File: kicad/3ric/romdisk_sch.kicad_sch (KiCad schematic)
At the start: 54 parts

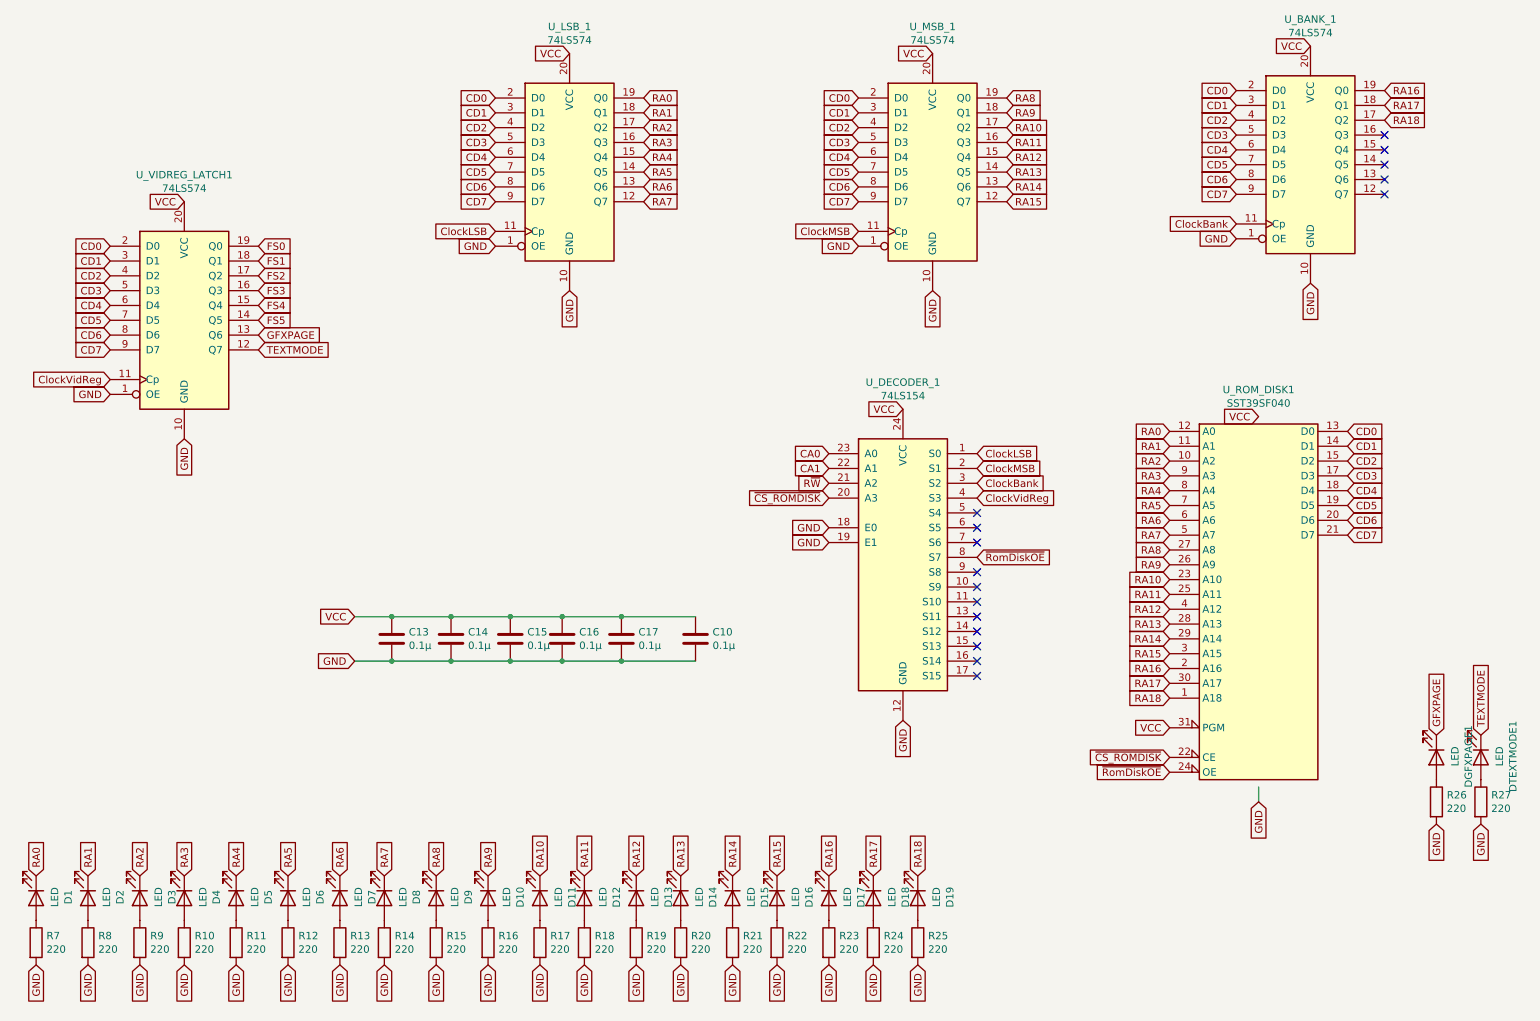
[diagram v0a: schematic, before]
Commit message: schematic updates - bring the schematics up to match breadboard changes current state has high res Apple II color emulation working
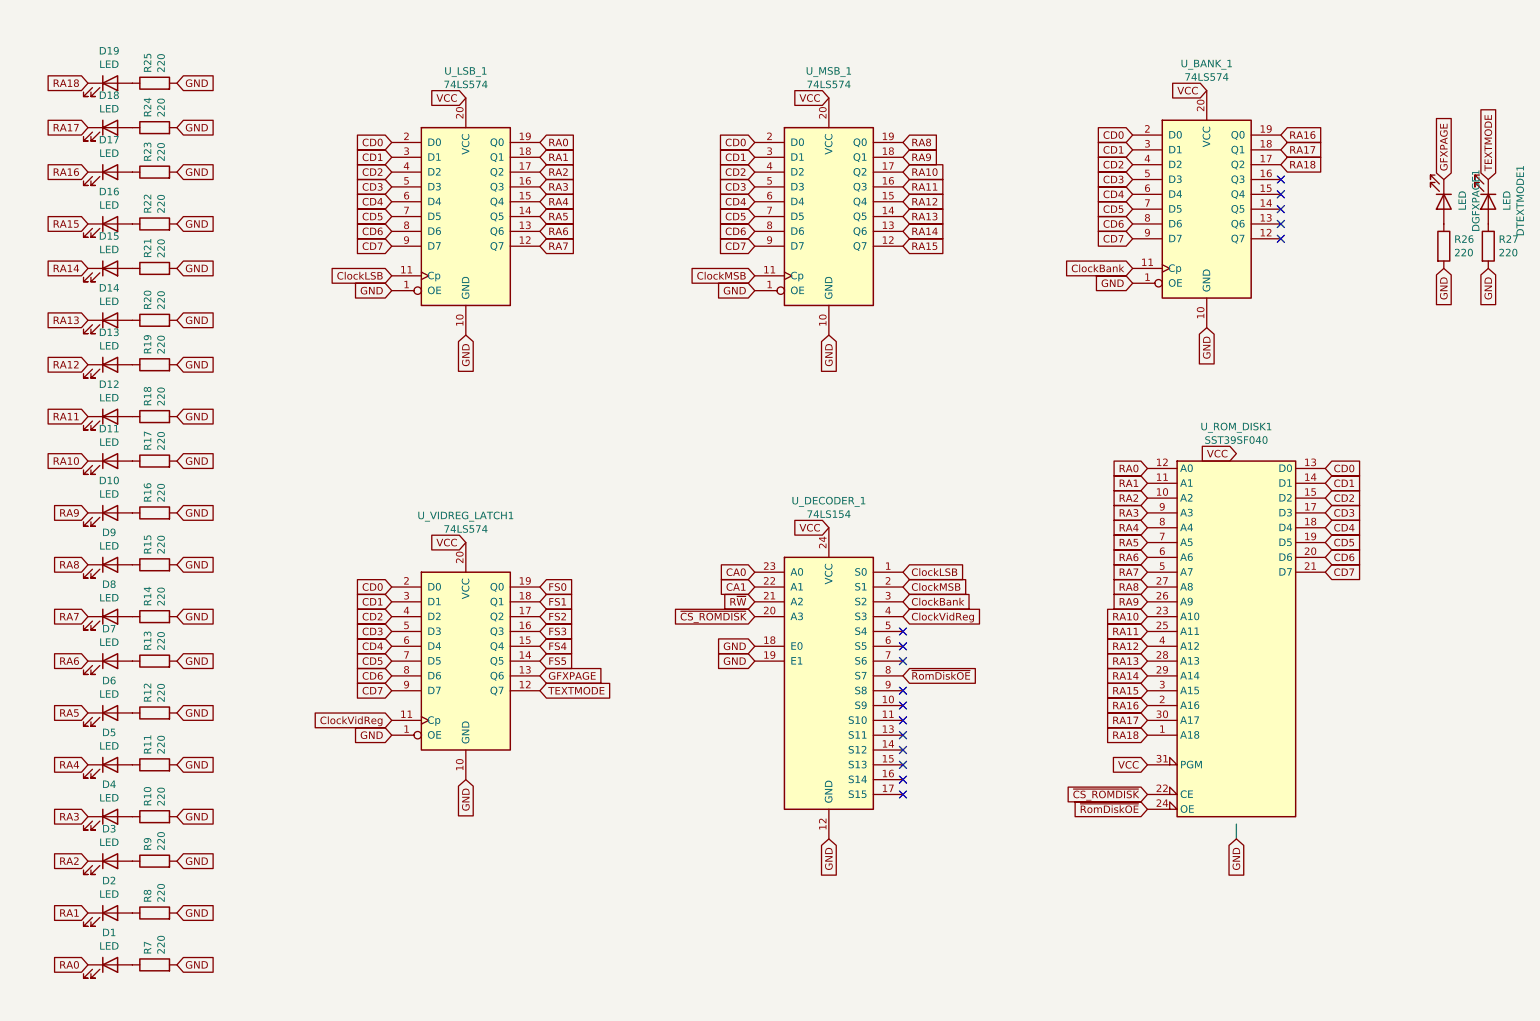
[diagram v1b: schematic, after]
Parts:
- removed C10, C13, C14, C15, C16, C17: 0.1µ, Capacitor_THT:C_Axial_L3.8mm_D2.6mm_P7.50mm_Horizontal, symbol Device:C
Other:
- moved on the sheet: D1, D10, D11, D12, D13, D14, D15, D16, D17, D18, D19, D2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

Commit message: updates to logisim project and schematics
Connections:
- net GFXPAGE: no longer U_VIDREG_LATCH1.13 (Q6)
- net TEXTMODE: no longer U_VIDREG_LATCH1.12 (Q7)
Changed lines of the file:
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@@
-    )
-  )
-  (global_label "TEXTMODE" (shape input) (at 107.95 130.81 0) (fields_autoplaced)
-    (effects (font (size 1.27 1.27)) (justify left))
-    (property "Intersheet References" "${INTERSHEET_REFS}" (id 0) (at 119.8579 130.7306 0)
-      (effects (font (size 1.27 1.27)) (justify left) hide)
     )
   )
@@
     )
   )
-  (global_label "GFXPAGE" (shape input) (at 107.95 128.27 0) (fields_autoplaced)
-    (effects (font (size 1.27 1.27)) (justify left))
-    (property "Intersheet References" "${INTERSHEET_REFS}" (id 0) (at 118.7088 128.1906 0)
-      (effects (font (size 1.27 1.27)) (justify left) hide)
-    )
-  )

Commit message: update schematics
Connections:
- net FS6: now reaches U_VIDREG_LATCH1.13 (Q6)
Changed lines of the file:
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@@
 (kicad_sch (version 20211123) (generator eeschema)
   (paper "A4")
-  (no_connect (at 170.18 130.81))
   (no_connect (at 170.18 148.59))
   (no_connect (at 170.18 140.97))
   (no_connect (at 170.18 133.35))
   (no_connect (at 170.18 135.89))
+  (no_connect (at 170.18 130.81))
   (no_connect (at 170.18 146.05))
   (no_connect (at 170.18 143.51))
@@
     )
   )
+  (global_label "~{RomDiskOE}" (shape input) (at 170.18 128.27 0) (fields_autoplaced)
+    (effects (font (size 1.27 1.27)) (justify left))
+    (property "Intersheet References" "${INTERSHEET_REFS}" (id 0) (at -8.89 11.43 0)
+      (effects (font (size 1.27 1.27)) hide)
+    )
+  )
   (global_label "GND" (shape input) (at 209.55 60.96 180) (fields_autoplaced)
     (effects (font (size 1.27 1.27)) (justify right))
@@
     )
   )
+  (global_label "FS6" (shape input) (at 107.95 128.27 0) (fields_autoplaced)
+    (effects (font (size 1.27 1.27)) (justify left))
+    (property "Intersheet References" "${INTERSHEET_REFS}" (id 0) (at 113.8707 128.1906 0)
+      (effects (font (size 1.27 1.27)) (justify left) hide)
+    )
+  )
   (global_label "RA8" (shape input) (at 30.48 109.22 180) (fields_autoplaced)
     (effects (font (size 1.27 1.27)) (justify right))
@@
     )
   )
-  (global_label "~{RomDiskOE}" (shape input) (at 170.18 128.27 0) (fields_autoplaced)
-    (effects (font (size 1.27 1.27)) (justify left))
-    (property "Intersheet References" "${INTERSHEET_REFS}" (id 0) (at -8.89 11.43 0)
-      (effects (font (size 1.27 1.27)) hide)
-    )
-  )

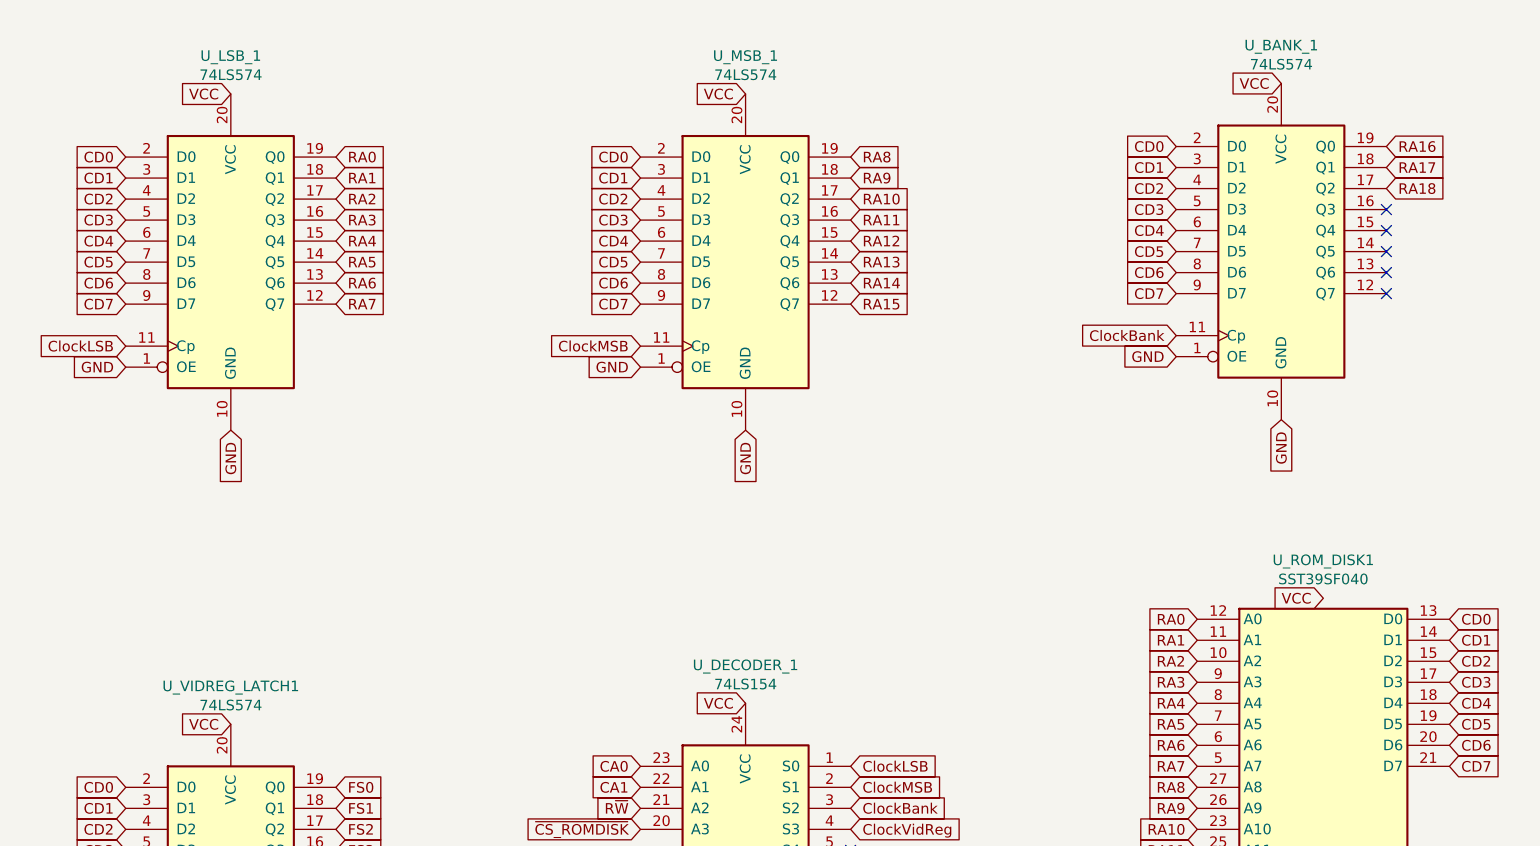
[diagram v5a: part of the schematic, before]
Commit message: update schematic based on breadboard
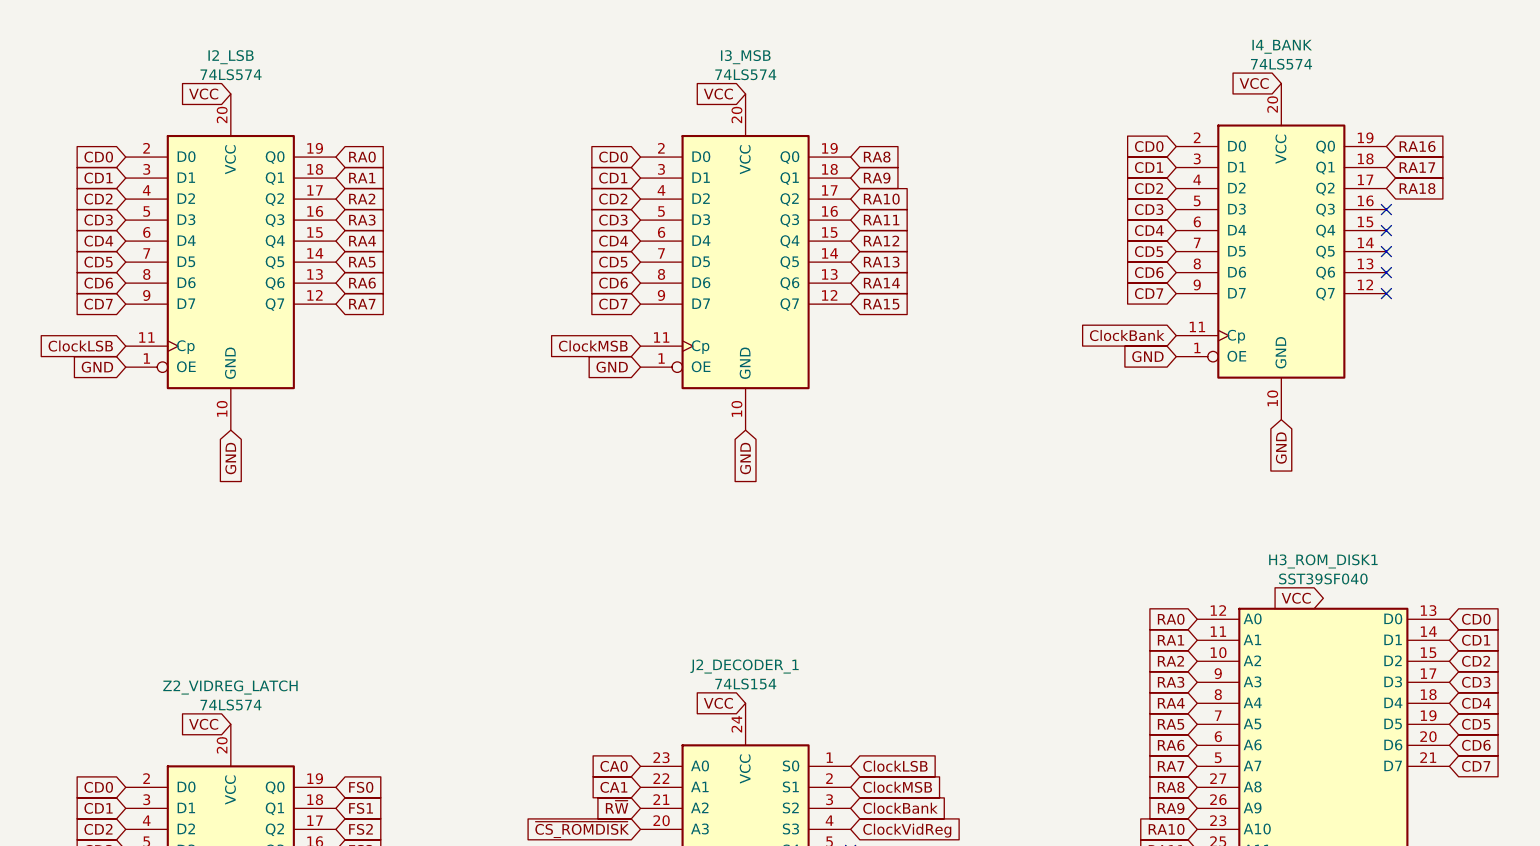
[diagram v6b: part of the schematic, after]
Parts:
- renumbered U_ROM_DISK1 to H3_ROM_DISK1, U_LSB_1 to I2_LSB, U_MSB_1 to I3_MSB, U_BANK_1 to I4_BANK, U_DECODER_1 to J2_DECODER_1, U_VIDREG_LATCH1 to Z2_VIDREG_LATCH
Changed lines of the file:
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@@
 		(on_board yes)
 		(dnp no)
-		(property "Reference" "U_LSB_1"
+		(property "Reference" "I2_LSB"
 			(at 95.25 24.6126 0)
 			(effects
@@
 			(project "3ric"
 				(path "/e63e39d7-6ac0-4ffd-8aa3-1841a4541b55/290c257d-4d63-492d-a5ad-035c64fcf51c"
-					(reference "U_LSB_1")
+					(reference "I2_LSB")
 					(unit 1)
 				)
@@
 		(on_board yes)
 		(dnp no)
-		(property "Reference" "U_ROM_DISK1"
+		(property "Reference" "H3_ROM_DISK1"
 			(at 227.33 85.5726 0)
 			(effects
@@
 			(project "3ric"
 				(path "/e63e39d7-6ac0-4ffd-8aa3-1841a4541b55/290c257d-4d63-492d-a5ad-035c64fcf51c"
-					(reference "U_ROM_DISK1")
+					(reference "H3_ROM_DISK1")
 					(unit 1)
 				)
@@
 		(on_board yes)
 		(dnp no)
-		(property "Reference" "U_MSB_1"
+		(property "Reference" "I3_MSB"
 			(at 157.48 24.6126 0)
 			(effects
@@
 			(project "3ric"
 				(path "/e63e39d7-6ac0-4ffd-8aa3-1841a4541b55/290c257d-4d63-492d-a5ad-035c64fcf51c"
-					(reference "U_MSB_1")
+					(reference "I3_MSB")
 					(unit 1)
 				)
@@
 		(on_board yes)
 		(dnp no)
-		(property "Reference" "U_VIDREG_LATCH1"
+		(property "Reference" "Z2_VIDREG_LATCH"
 			(at 95.25 100.8126 0)
 			(effects
@@
 			(project "3ric"
 				(path "/e63e39d7-6ac0-4ffd-8aa3-1841a4541b55/290c257d-4d63-492d-a5ad-035c64fcf51c"
-					(reference "U_VIDREG_LATCH1")
+					(reference "Z2_VIDREG_LATCH")
 					(unit 1)
 				)
@@
 		(on_board yes)
 		(dnp no)
-		(property "Reference" "U_BANK_1"
+		(property "Reference" "I4_BANK"
 			(at 222.25 23.3426 0)
 			(effects
@@
 			(project "3ric"
 				(path "/e63e39d7-6ac0-4ffd-8aa3-1841a4541b55/290c257d-4d63-492d-a5ad-035c64fcf51c"
-					(reference "U_BANK_1")
+					(reference "I4_BANK")
 					(unit 1)
 				)
@@
 		(on_board yes)
 		(dnp no)
-		(property "Reference" "U_DECODER_1"
+		(property "Reference" "J2_DECODER_1"
 			(at 157.48 98.2726 0)
 			(effects
@@
 			(project "3ric"
 				(path "/e63e39d7-6ac0-4ffd-8aa3-1841a4541b55/290c257d-4d63-492d-a5ad-035c64fcf51c"
-					(reference "U_DECODER_1")
+					(reference "J2_DECODER_1")
 					(unit 1)
 				)

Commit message: cleaning up of the schematic
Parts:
- removed DGFXPAGE1, DTEXTMODE1: LED, LED_THT:LED_D3.0mm, symbol Device:LED
- removed R26, R27: 220, Resistor_THT:R_Axial_DIN0207_L6.3mm_D2.5mm_P7.62mm_Horizontal, symbol Device:R
- renumbered I2_LSB to I2_LSB1, I3_MSB to I3_MSB1, I4_BANK to I4_BANK1, D1 to LED1, D10 to LED10, D11 to LED11, D12 to LED12, D13 to LED13, D14 to LED14, D15 to LED15, D16 to LED16, D17 to LED17, D18 to LED18, D19 to LED19, D2 to LED2, D3 to LED3, D4 to LED4, D5 to LED5, D6 to LED6, D7 to LED7, D8 to LED8, D9 to LED9, Z2_VIDREG_LATCH to Z2_VIDREG_LATCH1
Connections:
- net ROM2: now reaches Z2_VIDREG_LATCH1.12 (Q7)
- net FS6 renamed ROM1
